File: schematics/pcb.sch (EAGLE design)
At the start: 39 parts, among them IC1 7805TV, IC2 4050D, IC3 LP298XS, Q1 16Mhz, Q2 16Mhz, X1 MICROSD

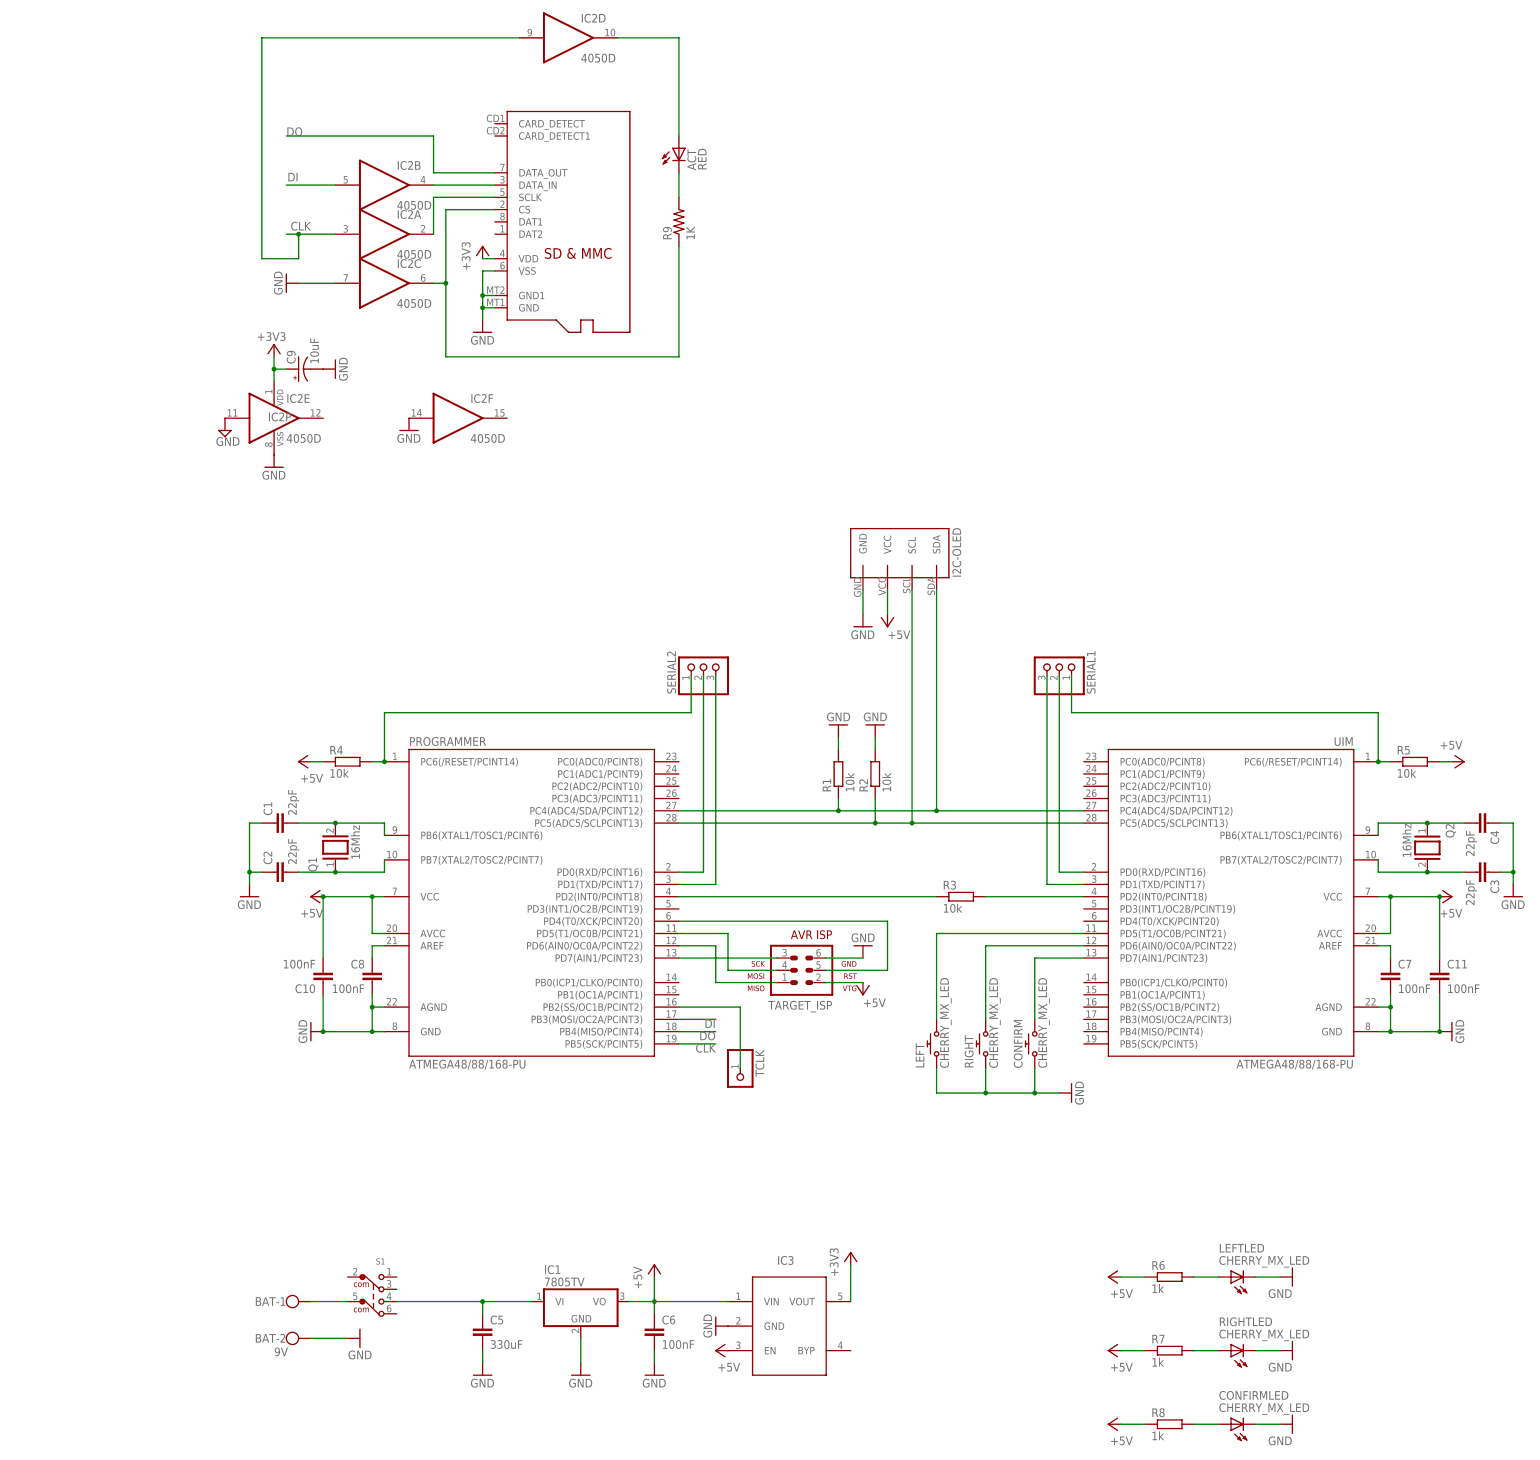
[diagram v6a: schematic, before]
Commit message: PCB part placements and partial routing
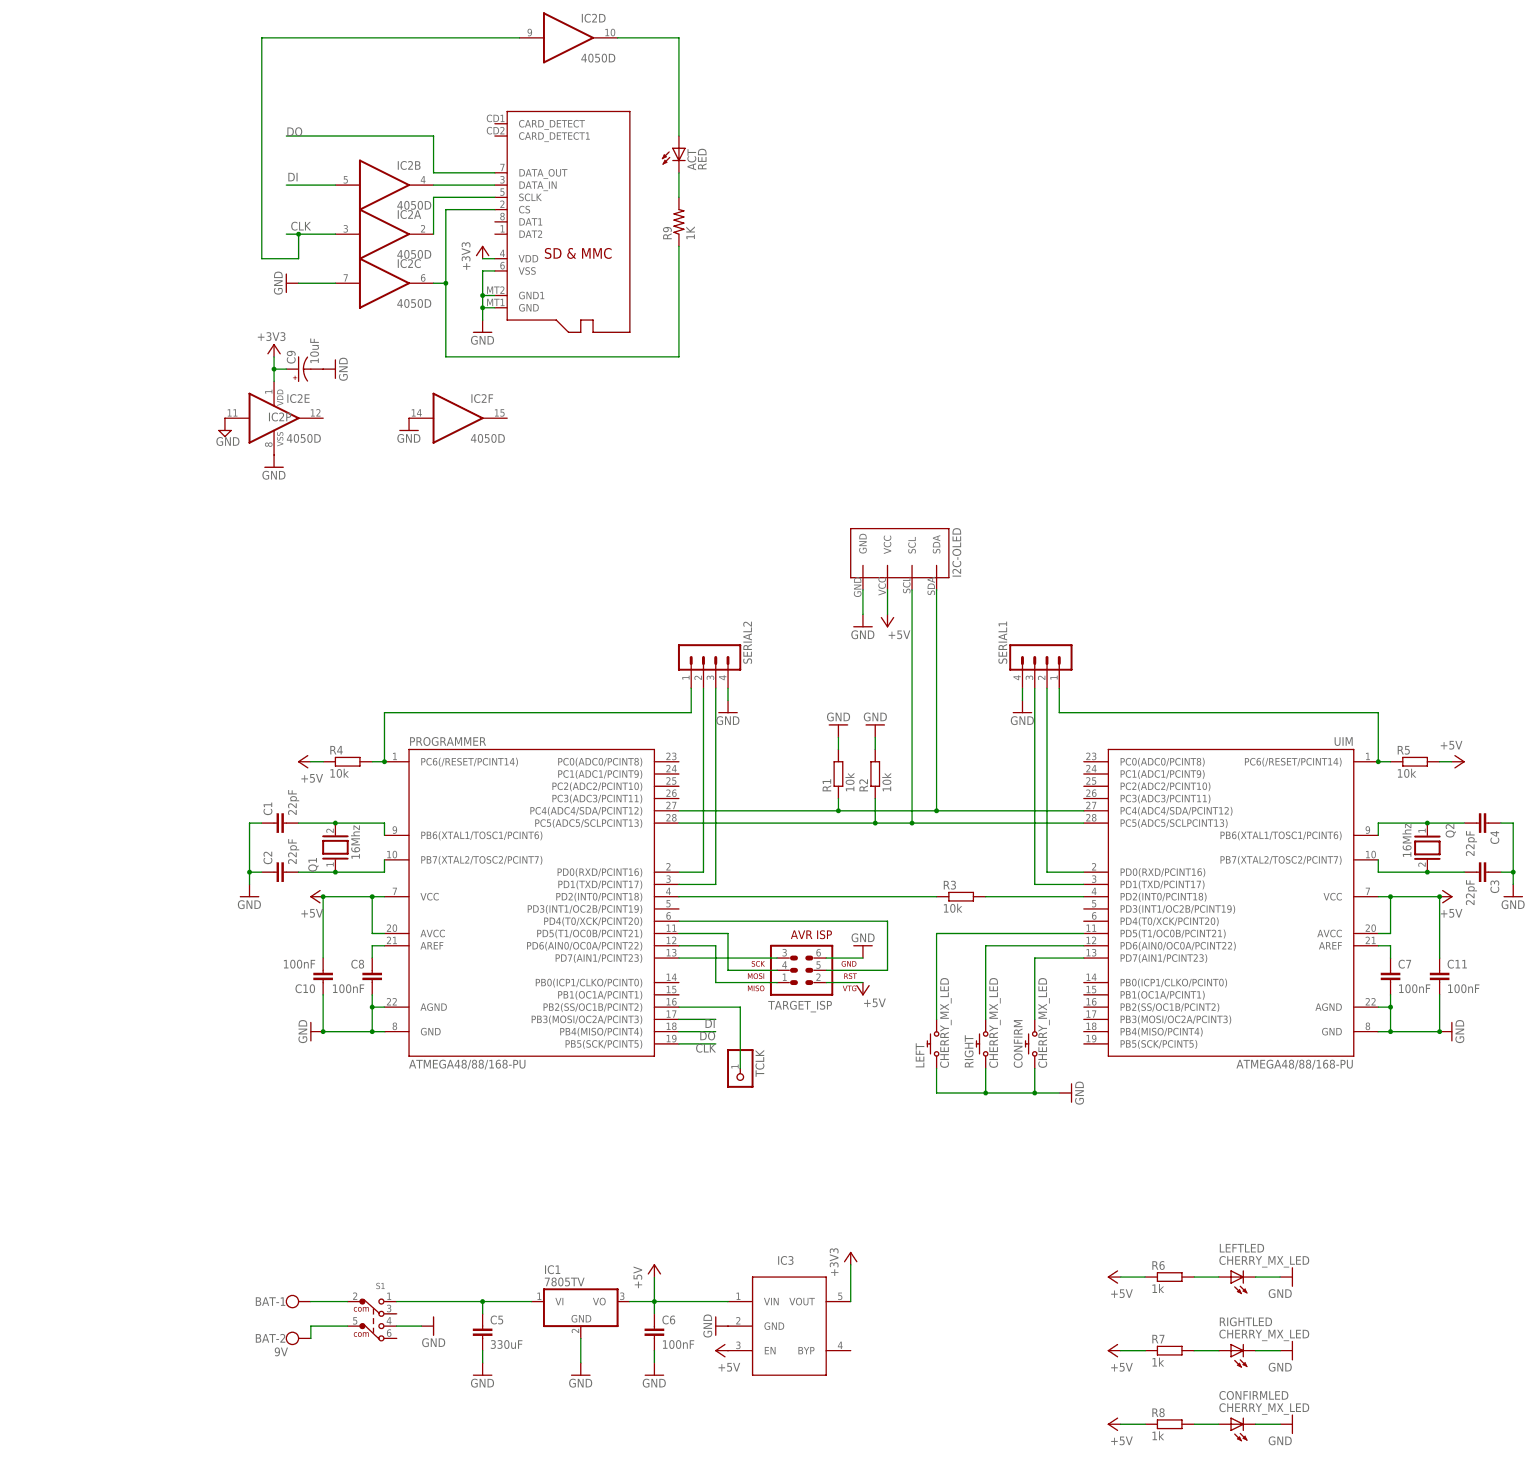
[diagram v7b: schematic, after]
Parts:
- SERIAL1, SERIAL2: device pinhead:PINHD-1X3 -> con-lstb:MA04-1
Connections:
- removed net N$17: BAT-1.KL, S1.COM1
- removed net PWRIN: C5.1, IC1.VI, S1.4
- new net 9V+: C5.1, IC1.VI, S1.1
- new net BAT+: BAT-1.KL, S1.COM
- new net BAT-: BAT-2.KL, S1.COM1
- net GND: now also S1.4, SERIAL1.4, SERIAL2.4; no longer BAT-2.KL
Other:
- moved on the sheet: S1
